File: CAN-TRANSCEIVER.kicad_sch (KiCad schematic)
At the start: 16 parts, among them IC2 ATA6561-GAQW-N

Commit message: First draft of component layout
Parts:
- U7: renamed from IC2; Arrow Part Number ATA6561-GAQW-N -> (none); Arrow Price/Stock https://www.arrow.com/en/products/ata6561-gaqw-n/microchip-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 -> (none); Height 1.75 -> (none); Manufacturer_Part_Number ATA6561-GAQW-N -> (none); Mouser Part Number 579-ATA6561-GAQW-N -> (none); Mouser Price/Stock https://www.mouser.co.uk/ProductDetail/Microchip-Technology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 -> (none)
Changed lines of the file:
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@@
   (symbol (lib_id "ESP32-S3_DB:ATA6561-GAQW-N") (at 134.62 95.885 0) (unit 1)
     (in_bom yes) (on_board yes) (dnp no) (fields_autoplaced)
-    (property "Reference" "IC2" (at 148.59 88.9 0)
+    (property "Reference" "U7" (at 148.59 88.9 0)
       (effects (font (size 1.27 1.27)))
     )
@@
       (effects (font (size 1.27 1.27)) (justify left top) hide)
     )
-    (property "Height" "1.75" (at 158.75 490.805 0)
-      (effects (font (size 1.27 1.27)) (justify left top) hide)
-    )
     (property "Manufacturer_Name" "Microchip" (at 158.75 590.805 0)
-      (effects (font (size 1.27 1.27)) (justify left top) hide)
-    )
-    (property "Manufacturer_Part_Number" "ATA6561-GAQW-N" (at 158.75 690.805 0)
-      (effects (font (size 1.27 1.27)) (justify left top) hide)
-    )
-    (property "Mouser Part Number" "579-ATA6561-GAQW-N" (at 158.75 790.805 0)
-      (effects (font (size 1.27 1.27)) (justify left top) hide)
-    )
-    (property "Mouser Price/Stock" "https://www.mouser.co.uk/ProductDetail/Microchip-Technology-Atmel/ATA6561-GAQW-N?qs=y6ZabgHbY%252BwGbm2JCZMHKQ%3D%3D" (at 158.75 890.805 0)
-      (effects (font (size 1.27 1.27)) (justify left top) hide)
-    )
-    (property "Arrow Part Number" "ATA6561-GAQW-N" (at 158.75 990.805 0)
-      (effects (font (size 1.27 1.27)) (justify left top) hide)
-    )
-    (property "Arrow Price/Stock" "https://www.arrow.com/en/products/ata6561-gaqw-n/microchip-technology?region=nac" (at 158.75 1090.805 0)
       (effects (font (size 1.27 1.27)) (justify left top) hide)
     )
@@
       (project "ESP32-S3_DB"
         (path "/b7fc4bd3-c219-4455-832b-8d795385dcf1/5968696a-d1c3-4df1-9868-cceeab327a7d"
-          (reference "IC2") (unit 1)
+          (reference "U7") (unit 1)
         )
       )

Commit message: Started ESP routing
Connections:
- net CAN_H renamed CAN_P
- net CAN_L renamed CAN_N
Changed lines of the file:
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@@
     (effects (font (size 1.27 1.27) (thickness 0.254) bold (color 0 0 255 1)) (justify left bottom))
   )
-  (label "CAN_H" (at 46.355 177.8 180) (fields_autoplaced)
+  (label "CAN_P" (at 46.355 177.8 180) (fields_autoplaced)
     (effects (font (size 1.27 1.27) bold (color 0 0 0 1)) (justify right bottom))
   )
@@
     (effects (font (size 1.27 1.27) bold (color 0 0 255 1)) (justify right bottom))
   )
-  (label "CAN_L" (at 263.525 99.06 180) (fields_autoplaced)
+  (label "CAN_N" (at 263.525 99.06 180) (fields_autoplaced)
     (effects (font (size 1.27 1.27) bold (color 0 0 0 1)) (justify right bottom))
   )
@@
     (effects (font (size 1.27 1.27) bold (color 255 0 0 1)) (justify right bottom))
   )
-  (label "CAN_L" (at 46.355 180.34 180) (fields_autoplaced)
+  (label "CAN_N" (at 46.355 180.34 180) (fields_autoplaced)
     (effects (font (size 1.27 1.27) bold (color 0 0 0 1)) (justify right bottom))
   )
@@
     (effects (font (size 1.27 1.27) bold (color 0 0 255 1)) (justify left bottom))
   )
-  (label "CAN_H" (at 263.525 93.98 180) (fields_autoplaced)
+  (label "CAN_P" (at 263.525 93.98 180) (fields_autoplaced)
     (effects (font (size 1.27 1.27) bold (color 0 0 0 1)) (justify right bottom))
   )
@@
     (effects (font (size 1.27 1.27) bold (color 0 0 255 1)) (justify left bottom))
   )
-  (hierarchical_label "CAN_L" (shape input) (at 33.655 180.34 180) (fields_autoplaced)
+  (hierarchical_label "CAN_N" (shape input) (at 33.655 180.34 180) (fields_autoplaced)
     (effects (font (size 1.27 1.27) bold (color 0 0 0 1)) (justify right))
   )
@@
     (effects (font (size 1.27 1.27) bold (color 255 0 0 1)) (justify right))
   )
-  (hierarchical_label "CAN_H" (shape input) (at 33.655 177.8 180) (fields_autoplaced)
+  (hierarchical_label "CAN_P" (shape input) (at 33.655 177.8 180) (fields_autoplaced)
     (effects (font (size 1.27 1.27) bold (color 0 0 0 1)) (justify right))
   )

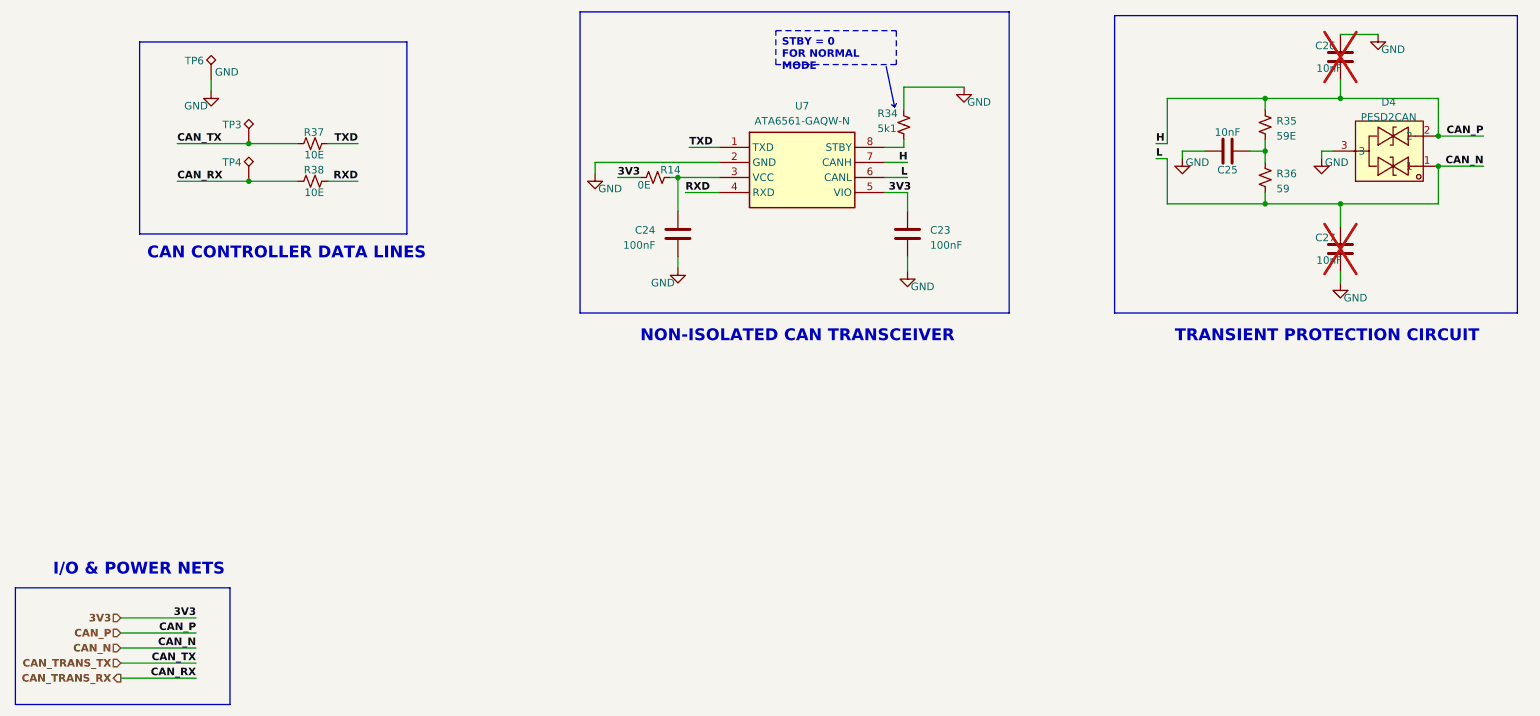
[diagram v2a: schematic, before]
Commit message: Changed GPIO mapping
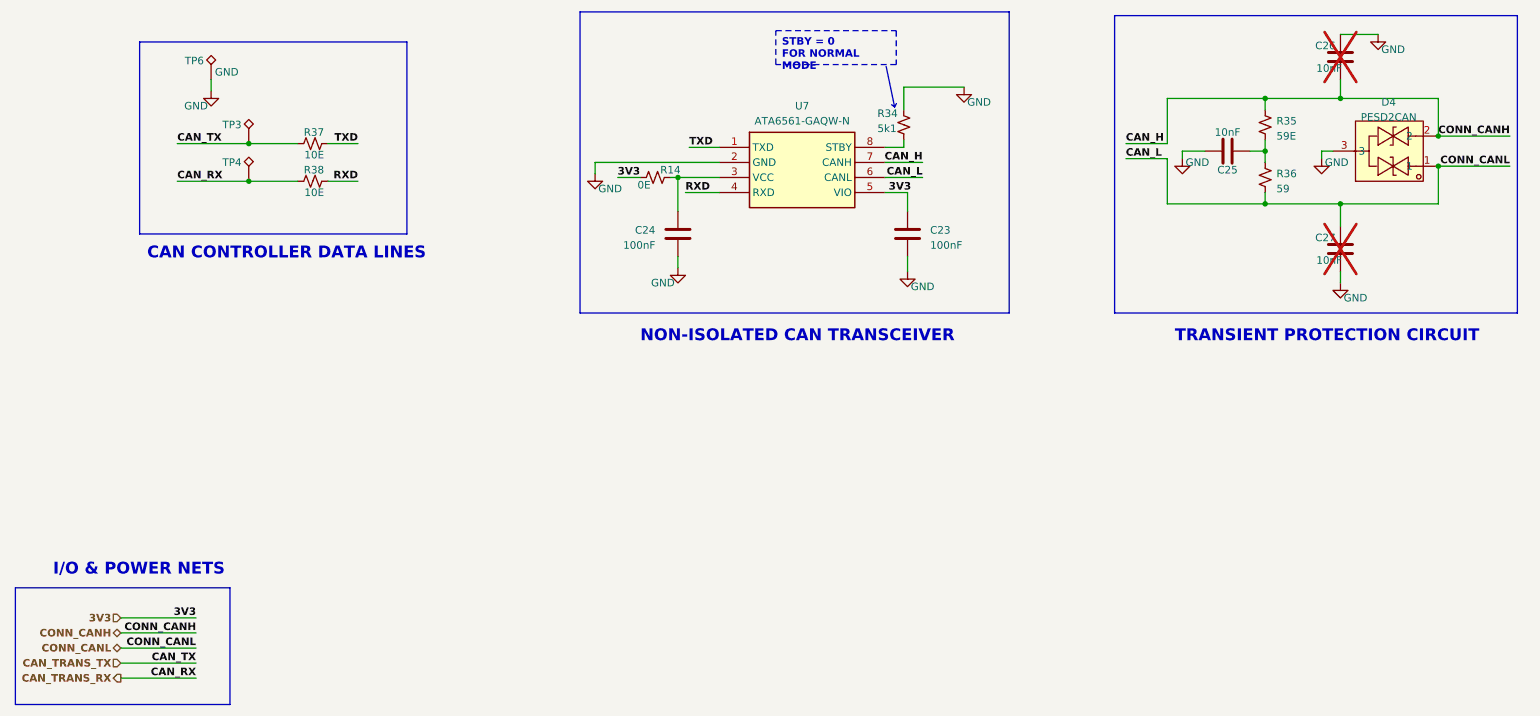
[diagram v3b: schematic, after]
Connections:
- net CAN_N renamed CONN_CANL
- net CAN_P renamed CONN_CANH
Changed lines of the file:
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@@
     (stroke (width 0.5) (type default) (color 0 0 0 1))
   )
-  (wire (pts (xy 166.37 98.425) (xy 162.56 98.425))
+  (wire (pts (xy 168.91 98.425) (xy 162.56 98.425))
     (stroke (width 0) (type default))
   )
@@
     (stroke (width 0) (type default))
   )
-  (wire (pts (xy 208.28 97.79) (xy 210.185 97.79))
+  (wire (pts (xy 203.2 97.79) (xy 210.185 97.79))
     (stroke (width 0) (type default))
   )
@@
     (stroke (width 1) (type default) (color 72 72 72 1))
   )
-  (wire (pts (xy 166.37 100.965) (xy 162.56 100.965))
-    (stroke (width 0) (type default))
-  )
-  (wire (pts (xy 255.905 93.98) (xy 263.525 93.98))
+  (wire (pts (xy 168.91 100.965) (xy 162.56 100.965))
+    (stroke (width 0) (type default))
+  )
+  (wire (pts (xy 255.905 93.98) (xy 267.97 93.98))
     (stroke (width 0) (type default))
   )
@@
     (stroke (width 1) (type default) (color 72 72 72 1))
   )
-  (wire (pts (xy 255.905 99.06) (xy 263.525 99.06))
+  (wire (pts (xy 255.905 99.06) (xy 267.97 99.06))
     (stroke (width 0) (type default))
   )
@@
     (stroke (width 0) (type default))
   )
-  (wire (pts (xy 208.28 95.25) (xy 210.185 95.25))
+  (wire (pts (xy 203.2 95.25) (xy 210.185 95.25))
     (stroke (width 0) (type default))
   )
@@
     (effects (font (size 1.27 1.27) bold (color 0 0 255 1)) (justify left bottom))
   )
-  (label "L" (at 208.28 97.79 0) (fields_autoplaced)
+  (label "CONN_CANH" (at 46.355 177.8 180) (fields_autoplaced)
+    (effects (font (size 1.27 1.27) bold (color 0 0 0 1)) (justify right bottom))
+  )
+  (label "CAN_H" (at 203.2 95.25 0) (fields_autoplaced)
     (effects (font (size 1.27 1.27) (thickness 0.254) bold (color 0 0 255 1)) (justify left bottom))
   )
-  (label "H" (at 166.37 98.425 180) (fields_autoplaced)
+  (label "CAN_H" (at 168.91 98.425 180) (fields_autoplaced)
     (effects (font (size 1.27 1.27) (thickness 0.254) bold (color 0 0 255 1)) (justify right bottom))
   )
-  (label "H" (at 208.28 95.25 0) (fields_autoplaced)
+  (label "CAN_L" (at 203.2 97.79 0) (fields_autoplaced)
     (effects (font (size 1.27 1.27) (thickness 0.254) bold (color 0 0 255 1)) (justify left bottom))
   )
-  (label "CAN_P" (at 46.355 177.8 180) (fields_autoplaced)
+  (label "CONN_CANL" (at 46.355 180.34 180) (fields_autoplaced)
     (effects (font (size 1.27 1.27) bold (color 0 0 0 1)) (justify right bottom))
   )
@@
     (effects (font (size 1.27 1.27) bold (color 0 0 255 1)) (justify right bottom))
   )
-  (label "CAN_N" (at 263.525 99.06 180) (fields_autoplaced)
+  (label "CONN_CANL" (at 267.97 99.06 180) (fields_autoplaced)
     (effects (font (size 1.27 1.27) bold (color 0 0 0 1)) (justify right bottom))
   )
@@
     (effects (font (size 1.27 1.27) bold (color 255 0 0 1)) (justify right bottom))
   )
-  (label "CAN_N" (at 46.355 180.34 180) (fields_autoplaced)
-    (effects (font (size 1.27 1.27) bold (color 0 0 0 1)) (justify right bottom))
-  )
   (label "CAN_RX" (at 46.355 185.42 180) (fields_autoplaced)
     (effects (font (size 1.27 1.27) bold (color 0 0 255 1)) (justify right bottom))
@@
     (effects (font (size 1.27 1.27) bold (color 0 0 255 1)) (justify left bottom))
   )
-  (label "CAN_P" (at 263.525 93.98 180) (fields_autoplaced)
+  (label "CONN_CANH" (at 267.97 93.98 180) (fields_autoplaced)
     (effects (font (size 1.27 1.27) bold (color 0 0 0 1)) (justify right bottom))
   )
@@
     (effects (font (size 1.27 1.27) bold (color 255 0 0 1)) (justify left bottom))
   )
-  (label "L" (at 166.37 100.965 180) (fields_autoplaced)
+  (label "CAN_L" (at 168.91 100.965 180) (fields_autoplaced)
     (effects (font (size 1.27 1.27) (thickness 0.254) bold (color 0 0 255 1)) (justify right bottom))
   )
@@
     (effects (font (size 1.27 1.27) bold (color 0 0 255 1)) (justify left bottom))
   )
-  (hierarchical_label "CAN_N" (shape input) (at 33.655 180.34 180) (fields_autoplaced)
+  (hierarchical_label "CONN_CANL" (shape bidirectional) (at 33.655 180.34 180) (fields_autoplaced)
     (effects (font (size 1.27 1.27) bold (color 0 0 0 1)) (justify right))
   )
@@
     (effects (font (size 1.27 1.27) bold (color 255 0 0 1)) (justify right))
   )
-  (hierarchical_label "CAN_P" (shape input) (at 33.655 177.8 180) (fields_autoplaced)
+  (hierarchical_label "CONN_CANH" (shape bidirectional) (at 33.655 177.8 180) (fields_autoplaced)
     (effects (font (size 1.27 1.27) bold (color 0 0 0 1)) (justify right))
   )

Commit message: Merge changes upstream
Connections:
- net CONN_CANH renamed CAN_P
- net CONN_CANL renamed CAN_N
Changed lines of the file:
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@@
     (stroke (width 0.5) (type default) (color 0 0 0 1))
   )
-  (wire (pts (xy 168.91 98.425) (xy 162.56 98.425))
+  (wire (pts (xy 166.37 98.425) (xy 162.56 98.425))
     (stroke (width 0) (type default))
   )
@@
     (stroke (width 0) (type default))
   )
-  (wire (pts (xy 203.2 97.79) (xy 210.185 97.79))
+  (wire (pts (xy 208.28 97.79) (xy 210.185 97.79))
     (stroke (width 0) (type default))
   )
@@
     (stroke (width 1) (type default) (color 72 72 72 1))
   )
-  (wire (pts (xy 168.91 100.965) (xy 162.56 100.965))
-    (stroke (width 0) (type default))
-  )
-  (wire (pts (xy 255.905 93.98) (xy 267.97 93.98))
+  (wire (pts (xy 166.37 100.965) (xy 162.56 100.965))
+    (stroke (width 0) (type default))
+  )
+  (wire (pts (xy 255.905 93.98) (xy 263.525 93.98))
     (stroke (width 0) (type default))
   )
@@
     (stroke (width 1) (type default) (color 72 72 72 1))
   )
-  (wire (pts (xy 255.905 99.06) (xy 267.97 99.06))
+  (wire (pts (xy 255.905 99.06) (xy 263.525 99.06))
     (stroke (width 0) (type default))
   )
@@
     (stroke (width 0) (type default))
   )
-  (wire (pts (xy 203.2 95.25) (xy 210.185 95.25))
+  (wire (pts (xy 208.28 95.25) (xy 210.185 95.25))
     (stroke (width 0) (type default))
   )
@@
     (effects (font (size 1.27 1.27) bold (color 0 0 255 1)) (justify left bottom))
   )
-  (label "CONN_CANH" (at 46.355 177.8 180) (fields_autoplaced)
-    (effects (font (size 1.27 1.27) bold (color 0 0 0 1)) (justify right bottom))
-  )
-  (label "CAN_H" (at 203.2 95.25 0) (fields_autoplaced)
+  (label "L" (at 208.28 97.79 0) (fields_autoplaced)
     (effects (font (size 1.27 1.27) (thickness 0.254) bold (color 0 0 255 1)) (justify left bottom))
   )
-  (label "CAN_H" (at 168.91 98.425 180) (fields_autoplaced)
+  (label "H" (at 166.37 98.425 180) (fields_autoplaced)
     (effects (font (size 1.27 1.27) (thickness 0.254) bold (color 0 0 255 1)) (justify right bottom))
   )
-  (label "CAN_L" (at 203.2 97.79 0) (fields_autoplaced)
+  (label "H" (at 208.28 95.25 0) (fields_autoplaced)
     (effects (font (size 1.27 1.27) (thickness 0.254) bold (color 0 0 255 1)) (justify left bottom))
   )
-  (label "CONN_CANL" (at 46.355 180.34 180) (fields_autoplaced)
+  (label "CAN_P" (at 46.355 177.8 180) (fields_autoplaced)
     (effects (font (size 1.27 1.27) bold (color 0 0 0 1)) (justify right bottom))
   )
@@
     (effects (font (size 1.27 1.27) bold (color 0 0 255 1)) (justify right bottom))
   )
-  (label "CONN_CANL" (at 267.97 99.06 180) (fields_autoplaced)
+  (label "CAN_N" (at 263.525 99.06 180) (fields_autoplaced)
     (effects (font (size 1.27 1.27) bold (color 0 0 0 1)) (justify right bottom))
   )
@@
     (effects (font (size 1.27 1.27) bold (color 255 0 0 1)) (justify right bottom))
   )
+  (label "CAN_N" (at 46.355 180.34 180) (fields_autoplaced)
+    (effects (font (size 1.27 1.27) bold (color 0 0 0 1)) (justify right bottom))
+  )
   (label "CAN_RX" (at 46.355 185.42 180) (fields_autoplaced)
     (effects (font (size 1.27 1.27) bold (color 0 0 255 1)) (justify right bottom))
@@
     (effects (font (size 1.27 1.27) bold (color 0 0 255 1)) (justify left bottom))
   )
-  (label "CONN_CANH" (at 267.97 93.98 180) (fields_autoplaced)
+  (label "CAN_P" (at 263.525 93.98 180) (fields_autoplaced)
     (effects (font (size 1.27 1.27) bold (color 0 0 0 1)) (justify right bottom))
   )
@@
     (effects (font (size 1.27 1.27) bold (color 255 0 0 1)) (justify left bottom))
   )
-  (label "CAN_L" (at 168.91 100.965 180) (fields_autoplaced)
+  (label "L" (at 166.37 100.965 180) (fields_autoplaced)
     (effects (font (size 1.27 1.27) (thickness 0.254) bold (color 0 0 255 1)) (justify right bottom))
   )
@@
     (effects (font (size 1.27 1.27) bold (color 0 0 255 1)) (justify left bottom))
   )
-  (hierarchical_label "CONN_CANL" (shape bidirectional) (at 33.655 180.34 180) (fields_autoplaced)
+  (hierarchical_label "CAN_N" (shape input) (at 33.655 180.34 180) (fields_autoplaced)
     (effects (font (size 1.27 1.27) bold (color 0 0 0 1)) (justify right))
   )
@@
     (effects (font (size 1.27 1.27) bold (color 255 0 0 1)) (justify right))
   )
-  (hierarchical_label "CONN_CANH" (shape bidirectional) (at 33.655 177.8 180) (fields_autoplaced)
+  (hierarchical_label "CAN_P" (shape input) (at 33.655 177.8 180) (fields_autoplaced)
     (effects (font (size 1.27 1.27) bold (color 0 0 0 1)) (justify right))
   )

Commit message: Added HW-Tinkerers logo and supporting graphics
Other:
- company: (none) -> HW-TINKERERS (hw.tinkerers@gmail.com)
- title: (none) -> HARDWARE TINKERERS ESP32-S3 DB
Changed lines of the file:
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@@
 (kicad_sch (version 20230121) (generator eeschema)
   (paper "A4")
+  (title_block
+    (title "HARDWARE TINKERERS ESP32-S3 DB")
+    (rev "1.0.0")
+    (company "HW-TINKERERS (hw.tinkerers@gmail.com)")
+    (comment 1 "Email: bhandarkasrishtikr111@gmail.com")
+    (comment 2 "Author: Srishtik Bhandarkar")
+    (comment 3 "Email: vaibhavkhatri00@gmail.com")
+    (comment 4 "Author: Vaibhav Khatri")
+    (comment 5 "Official HW-Tinkerers email: hw.tinkerers@gmail.com")
+  )
   (junction (at 255.905 93.98) (diameter 0) (color 0 0 0 0)
   )
